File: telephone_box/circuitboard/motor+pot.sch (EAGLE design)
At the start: 10 parts, among them J2 TERM-1X02-FABLAB, J3 JACK-2.1MM

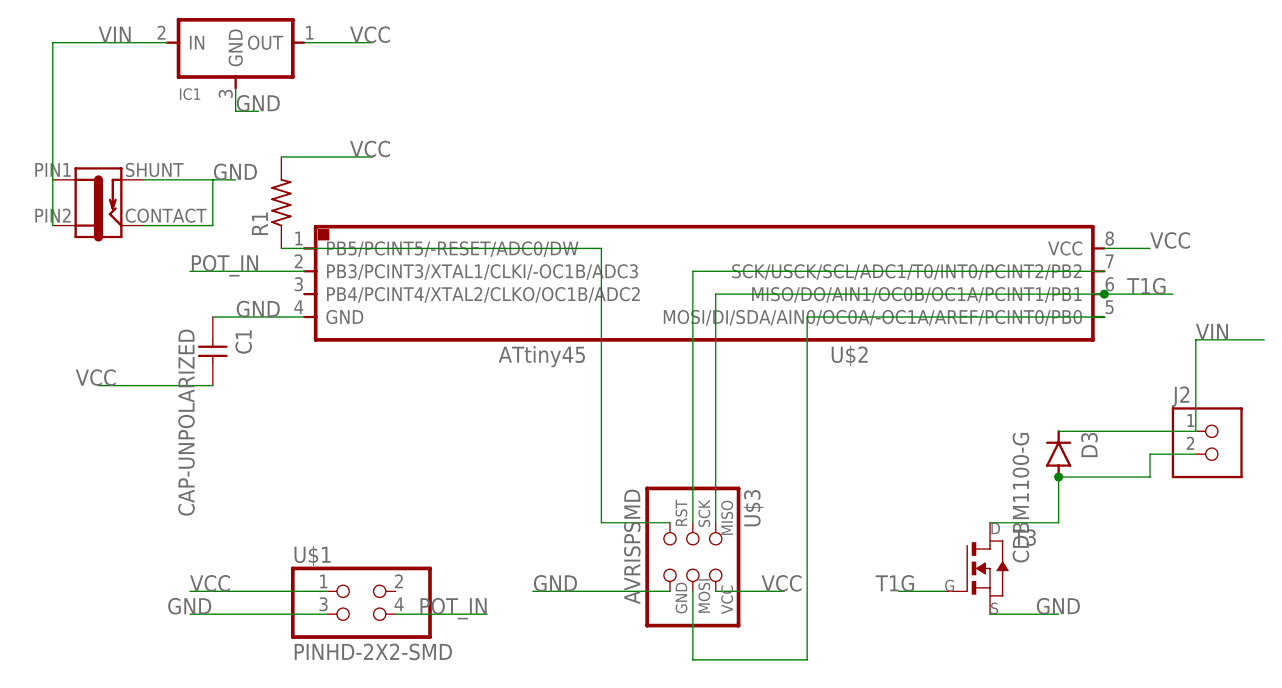
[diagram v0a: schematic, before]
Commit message: moved stepper out and edited telophone
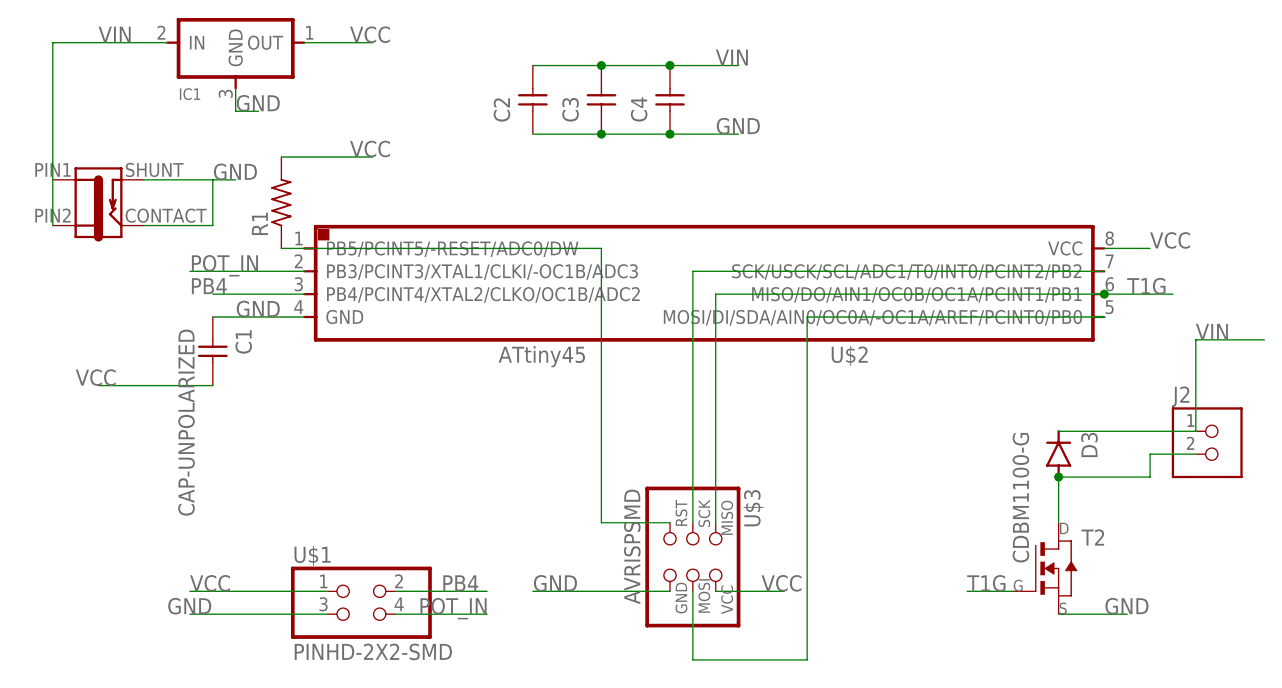
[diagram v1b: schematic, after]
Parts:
- removed T3: (no value), fab:MOSFET_NTO252
- added C2, C3, C4: (no value), fab:CAP-UNPOLARIZED
- added T2: (no value), fab:NMOSFETTO252
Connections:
- removed net N$2: D3.ANODE, J2.2, T3.D
- new net N$10: D3.ANODE, J2.2, T2.D
- new net PB4: U$1.2, U$2.PB4/PCINT4/XTAL2/CLKO/OC1B/ADC2
- net GND: now also C2.1, C3.1, C4.1, T2.S; no longer T3.S
- net T1G: now also T2.G; no longer T3.G
- net VIN: now also C2.2, C3.2, C4.2
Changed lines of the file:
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@@
 <layer number="59" name="tCarbon" color="7" fill="1" visible="no" active="no"/>
 <layer number="60" name="bCarbon" color="7" fill="1" visible="no" active="no"/>
-<layer number="88" name="SimResults" color="9" fill="1" visible="yes" active="yes"/>
-<layer number="89" name="SimProbes" color="9" fill="1" visible="yes" active="yes"/>
 <layer number="90" name="Modules" color="5" fill="1" visible="yes" active="yes"/>
 <layer number="91" name="Nets" color="2" fill="1" visible="yes" active="yes"/>
@@
 <layer number="115" name="ReferenceISLANDS" color="7" fill="1" visible="no" active="yes"/>
 <layer number="116" name="Patch_BOT" color="9" fill="4" visible="no" active="yes"/>
-<layer number="117" name="BACKMAAT1" color="7" fill="1" visible="yes" active="yes"/>
 <layer number="118" name="Rect_Pads" color="7" fill="1" visible="no" active="yes"/>
-<layer number="119" name="KAP_TEKEN" color="7" fill="1" visible="yes" active="yes"/>
-<layer number="120" name="KAP_MAAT1" color="7" fill="1" visible="yes" active="yes"/>
 <layer number="121" name="_tsilk" color="7" fill="1" visible="no" active="yes"/>
 <layer number="122" name="_bsilk" color="7" fill="1" visible="no" active="yes"/>
@@
 <layer number="128" name="_bValues" color="7" fill="1" visible="no" active="yes"/>
 <layer number="129" name="Mask" color="7" fill="1" visible="no" active="yes"/>
-<layer number="130" name="SMDSTROOK" color="7" fill="1" visible="yes" active="yes"/>
 <layer number="131" name="tAdjust" color="7" fill="1" visible="no" active="yes"/>
 <layer number="132" name="bAdjust" color="7" fill="1" visible="no" active="yes"/>
-<layer number="133" name="bottom_silk" color="7" fill="1" visible="yes" active="yes"/>
 <layer number="144" name="Drill_legend" color="7" fill="1" visible="no" active="yes"/>
 <layer number="150" name="Notes" color="7" fill="1" visible="no" active="yes"/>
@@
 <part name="U$1" library="fab" deviceset="PINHD-2X2-SMD" device=""/>
 <part name="J3" library="fab " deviceset="JACK-2.1MM" device=""/>
-<part name="T3" library="fab" deviceset="MOSFET_N" device="TO252"/>
+<part name="T2" library="fab" deviceset="NMOSFET" device="TO252"/>
+<part name="C2" library="fab" deviceset="CAP-UNPOLARIZED" device=""/>
+<part name="C3" library="fab" deviceset="CAP-UNPOLARIZED" device=""/>
+<part name="C4" library="fab" deviceset="CAP-UNPOLARIZED" device=""/>
 </parts>
 <sheets>
@@
 <instance part="U$1" gate="G$1" x="20.32" y="15.24"/>
 <instance part="J3" gate="G$1" x="-10.16" y="60.96"/>
-<instance part="T3" gate="A" x="88.9" y="20.32"/>
+<instance part="T2" gate="A" x="96.52" y="20.32"/>
+<instance part="C2" gate="&gt;NAME" x="38.1" y="73.66" rot="R90"/>
+<instance part="C3" gate="&gt;NAME" x="45.72" y="73.66" rot="R90"/>
+<instance part="C4" gate="&gt;NAME" x="53.34" y="73.66" rot="R90"/>
 </instances>
 <busses>
@@
 </segment>
 <segment>
-<pinref part="T3" gate="A" pin="S"/>
-<wire x1="88.9" y1="15.24" x2="96.52" y2="15.24" width="0.1524" layer="91"/>
-<label x="93.98" y="15.24" size="1.778" layer="95"/>
+<pinref part="T2" gate="A" pin="S"/>
+<wire x1="96.52" y1="15.24" x2="104.14" y2="15.24" width="0.1524" layer="91"/>
+<label x="101.6" y="15.24" size="1.778" layer="95"/>
+</segment>
+<segment>
+<pinref part="C2" gate="&gt;NAME" pin="1"/>
+<pinref part="C3" gate="&gt;NAME" pin="1"/>
+<wire x1="38.1" y1="68.58" x2="45.72" y2="68.58" width="0.1524" layer="91"/>
+<pinref part="C4" gate="&gt;NAME" pin="1"/>
+<wire x1="45.72" y1="68.58" x2="53.34" y2="68.58" width="0.1524" layer="91"/>
+<junction x="45.72" y="68.58"/>
+<wire x1="53.34" y1="68.58" x2="60.96" y2="68.58" width="0.1524" layer="91"/>
+<junction x="53.34" y="68.58"/>
+<label x="58.42" y="68.58" size="1.778" layer="95"/>
 </segment>
 </net>
@@
 </segment>
 <segment>
-<pinref part="T3" gate="A" pin="G"/>
-<wire x1="83.82" y1="17.78" x2="78.74" y2="17.78" width="0.1524" layer="91"/>
-<label x="76.2" y="17.78" size="1.778" layer="95"/>
+<pinref part="T2" gate="A" pin="G"/>
+<wire x1="91.44" y1="17.78" x2="86.36" y2="17.78" width="0.1524" layer="91"/>
+<label x="86.36" y="17.78" size="1.778" layer="95"/>
 </segment>
 </net>
@@
 <wire x1="101.6" y1="53.34" x2="55.88" y2="53.34" width="0.1524" layer="91"/>
 <wire x1="55.88" y1="53.34" x2="55.88" y2="25.4" width="0.1524" layer="91"/>
+</segment>
+</net>
+<net name="N$10" class="0">
+<segment>
+<pinref part="D3" gate="G$1" pin="ANODE"/>
+<wire x1="96.52" y1="30.48" x2="106.68" y2="30.48" width="0.1524" layer="91"/>
+<wire x1="106.68" y1="30.48" x2="106.68" y2="33.02" width="0.1524" layer="91"/>
+<pinref part="J2" gate="G$1" pin="2"/>
+<wire x1="106.68" y1="33.02" x2="111.76" y2="33.02" width="0.1524" layer="91"/>
+<junction x="96.52" y="30.48"/>
+<pinref part="T2" gate="A" pin="D"/>
+<wire x1="96.52" y1="25.4" x2="96.52" y2="30.48" width="0.1524" layer="91"/>
 </segment>
 </net>
@@
 <label x="111.76" y="45.72" size="1.778" layer="95"/>
 </segment>
-</net>
-<net name="N$2" class="0">
-<segment>
-<pinref part="T3" gate="A" pin="D"/>
-<wire x1="88.9" y1="25.4" x2="96.52" y2="25.4" width="0.1524" layer="91"/>
-<pinref part="D3" gate="G$1" pin="ANODE"/>
-<wire x1="96.52" y1="30.48" x2="106.68" y2="30.48" width="0.1524" layer="91"/>
-<wire x1="106.68" y1="30.48" x2="106.68" y2="33.02" width="0.1524" layer="91"/>
-<pinref part="J2" gate="G$1" pin="2"/>
-<wire x1="106.68" y1="33.02" x2="111.76" y2="33.02" width="0.1524" layer="91"/>
-<junction x="96.52" y="30.48"/>
-<wire x1="96.52" y1="25.4" x2="96.52" y2="30.48" width="0.1524" layer="91"/>
-</segment>
-</net>
+<segment>
+<pinref part="C2" gate="&gt;NAME" pin="2"/>
+<pinref part="C3" gate="&gt;NAME" pin="2"/>
+<wire x1="38.1" y1="76.2" x2="45.72" y2="76.2" width="0.1524" layer="91"/>
+<pinref part="C4" gate="&gt;NAME" pin="2"/>
+<wire x1="45.72" y1="76.2" x2="53.34" y2="76.2" width="0.1524" layer="91"/>
+<junction x="45.72" y="76.2"/>
+<wire x1="53.34" y1="76.2" x2="60.96" y2="76.2" width="0.1524" layer="91"/>
+<junction x="53.34" y="76.2"/>
+<label x="58.42" y="76.2" size="1.778" layer="95"/>
+</segment>
+</net>
+<net name="PB4" class="0">
+<segment>
+<pinref part="U$2" gate="G$1" pin="PB4/PCINT4/XTAL2/CLKO/OC1B/ADC2"/>
+<wire x1="12.7" y1="50.8" x2="2.54" y2="50.8" width="0.1524" layer="91"/>
+<label x="0" y="50.8" size="1.778" layer="95"/>
+</segment>
+<segment>
+<pinref part="U$1" gate="G$1" pin="2"/>
+<wire x1="22.86" y1="17.78" x2="33.02" y2="17.78" width="0.1524" layer="91"/>
+<label x="27.94" y="17.78" size="1.778" layer="95"/>
+</segment>
+</net>
